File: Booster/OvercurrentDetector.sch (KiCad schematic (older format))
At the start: 37 parts

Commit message: Removed need for enable signal replacing it with a missing pulse detection RC based circuit.
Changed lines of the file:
@@
 Connection ~ 2650 6150
 Wire Wire Line
-	2650 6050 2650 6150
-Wire Wire Line
-	2650 6150 2650 6250
+	2650 6050 2650 6250
 Wire Wire Line
 	2750 1400 2600 1400
@@
 	2600 1400 2600 1200
 Wire Wire Line
-	3050 2900 3900 2900
+	3050 2900 4400 2900
 Wire Wire Line
-	3900 2900 4400 2900
-Wire Wire Line
-	4100 1350 4100 1400
-Wire Wire Line
-	4100 1400 4100 1650
+	4100 1350 4100 1650
 Wire Wire Line
 	4100 1050 4100 1000
 Wire Wire Line
-	4100 1000 4300 1000
-Wire Wire Line
-	4300 1000 4500 1000
-Wire Wire Line
-	4500 1000 8350 1000
+	4100 1000 8350 1000
 Wire Wire Line
 	4300 1000 4300 1050
@@
 	4100 1650 4150 1650
 Wire Wire Line
-	4300 1350 4300 1400
+	4300 1350 4300 1500
 Wire Wire Line
-	4300 1400 4300 1500
+	4300 1800 4300 1900
 Wire Wire Line
-	4300 1800 4300 1850
-Wire Wire Line
-	4300 1850 4300 1900
-Wire Wire Line
-	3350 1400 3450 1400
-Wire Wire Line
-	3450 1400 4100 1400
-Wire Wire Line
-	4100 1400 4300 1400
+	3350 1400 4300 1400
 Wire Wire Line
 	4500 1000 4500 1900
@@
 	4700 2100 4900 2100
 Wire Wire Line
-	4900 1850 4900 2100
-Wire Wire Line
-	4900 2100 4900 2250
+	4900 1850 4900 2250
 Connection ~ 4900 2100
 Wire Wire Line
 	4900 2750 4900 2550
 Wire Wire Line
-	3050 1700 3050 2900
+	3050 1700 3050 3450
 Wire Wire Line
-	3050 2900 3050 3450
+	3050 3750 3050 4000
 Wire Wire Line
-	3050 3750 3050 3900
-Wire Wire Line
-	3050 3900 3050 4000
-Wire Wire Line
-	3250 3750 3250 3900
-Wire Wire Line
-	3250 3900 3250 4000
+	3250 3750 3250 4000
 Wire Wire Line
 	3250 2050 3250 3450
@@
 	2650 5750 2650 5450
 Wire Wire Line
-	2500 6800 2500 7000
-Wire Wire Line
-	2500 7000 2500 7100
+	2500 6800 2500 7100
 Wire Wire Line
 	2650 6650 2650 6550
@@
 Connection ~ 3150 4800
 Wire Wire Line
-	4300 6050 4600 6050
+	4300 6050 5300 6050
 Wire Wire Line
-	4600 6050 5300 6050
-Wire Wire Line
-	4600 5600 4600 6050
-Wire Wire Line
-	4600 6050 4600 6200
+	4600 5600 4600 6200
 Connection ~ 4600 6050
 Wire Wire Line
@@
 	4600 6500 4600 6850
 Wire Wire Line
-	3150 4600 3150 4800
-Wire Wire Line
-	3150 4800 3150 5950
+	3150 4600 3150 5950
 Wire Wire Line
 	3150 5950 3700 5950
@@
 	3600 5700 3600 5600
 Wire Wire Line
-	3900 4950 3900 5150
-Wire Wire Line
-	3900 5150 3900 5750
+	3900 4950 3900 5750
 Wire Wire Line
 	3600 5300 3600 5150
@@
 	3900 6350 3900 6850
 Wire Wire Line
-	5900 5950 5950 5950
-Wire Wire Line
-	5950 5950 6850 5950
+	5900 5950 6850 5950
 Wire Wire Line
 	6850 5950 6850 4900
@@
 	8250 4000 8550 4000
 Wire Wire Line
-	8550 3850 8550 4000
-Wire Wire Line
-	8550 4000 8550 4100
+	8550 3850 8550 4100
 Connection ~ 8550 4000
 Wire Wire Line
@@
 	8750 5100 9000 5100
 Wire Wire Line
-	9000 4500 9000 5100
+	9000 4500 9000 5550
 Wire Wire Line
-	9000 5100 9000 5300
-Wire Wire Line
-	9000 5300 9000 5550
-Wire Wire Line
-	8750 5300 9000 5300
-Wire Wire Line
-	9000 5300 9200 5300
+	8750 5300 9200 5300
 Connection ~ 9000 5300
 Connection ~ 9000 5100
@@
 	9250 4150 9000 4150
 Wire Wire Line
-	9000 3850 9000 4150
-Wire Wire Line
-	9000 4150 9000 4200
+	9000 3850 9000 4200
 Connection ~ 9000 4150
 Wire Wire Line
 	7400 5800 7400 6000
 Wire Wire Line
-	7400 6000 8250 6000
+	7400 6000 9000 6000
 Wire Wire Line
-	8250 6000 9000 6000
-Wire Wire Line
-	8250 5500 8250 6000
-Wire Wire Line
-	8250 6000 8250 6150
+	8250 5500 8250 6150
 Connection ~ 8250 6000
 $Comp

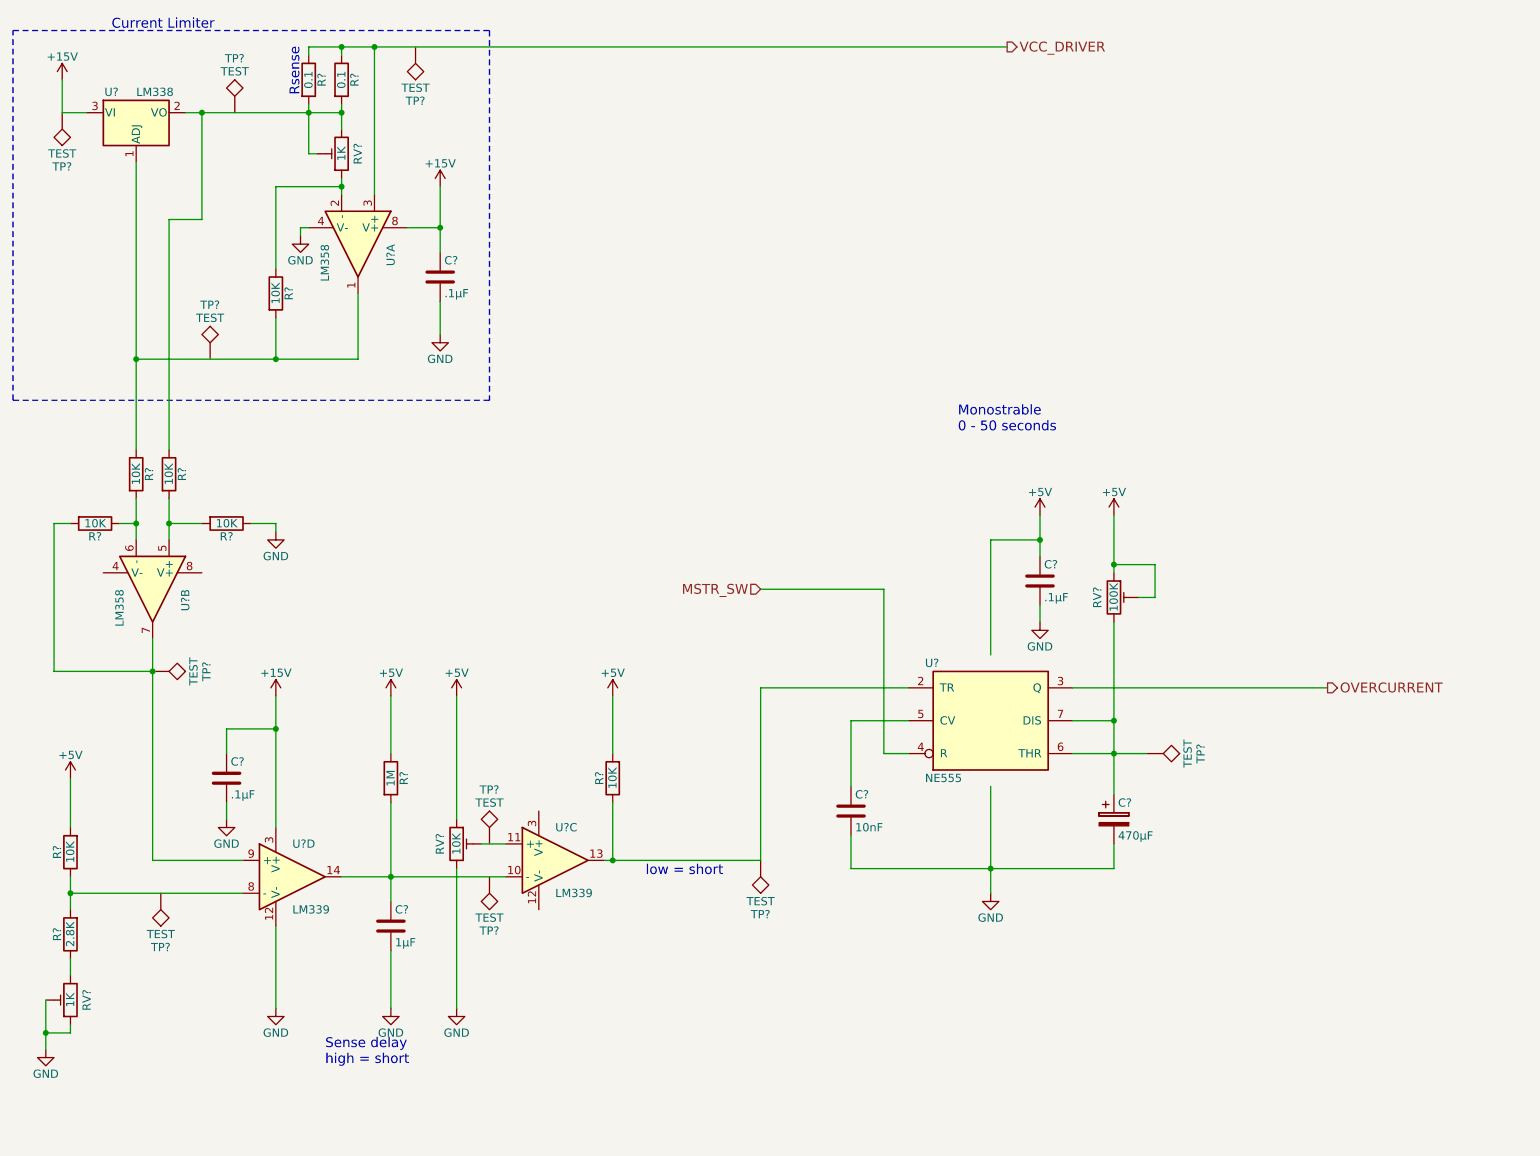
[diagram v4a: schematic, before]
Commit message: Fixed missing connections.
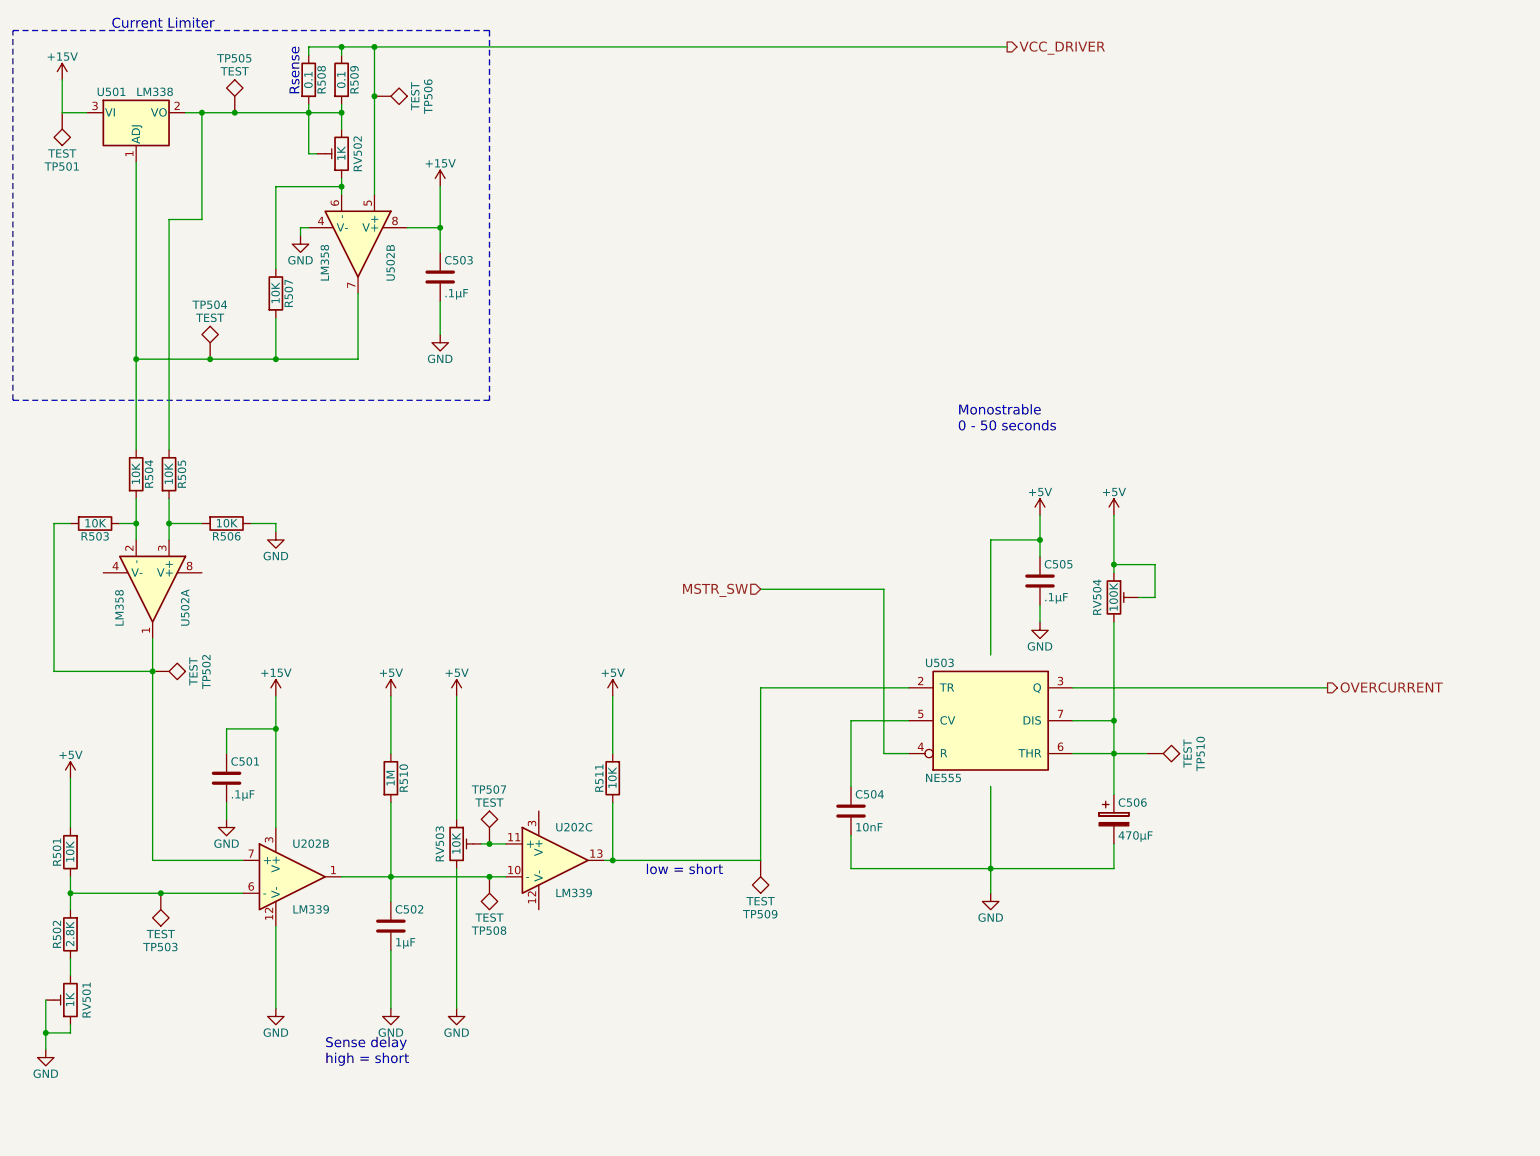
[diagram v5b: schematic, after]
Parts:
- gave numbers to parts that had none: 35
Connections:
- net VCC_DRIVER: now also TP506.1, U502.5 (+); no longer U502.3 (+)
- net at R501.1, R502.2: now also TP503.1, U202.6 (-); no longer U202.8 (-)
- net at R504.1, R507.2, U501.1 (ADJ): now also TP504.1, U502.7; no longer U502.1
- net at R505.1, R508.2, R509.2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: now also TP505.1
- net at R507.1, RV502.1: now also U502.6 (-); no longer U502.2 (-)
- net at R505.2, R506.2: now also U502.3 (+); no longer U502.5 (+)
- net at R503.1, R504.2: now also U502.2 (-); no longer U502.6 (-)
- net at R503.2, TP502.1: now also U202.7 (+), U502.1; no longer U202.9 (+), U502.7
- net at C502.1, R510.2, U202.10 (-): now also TP508.1, U202.1; no longer U202.14
- net at RV503.2, U202.11 (+): now also TP507.1
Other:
- moved on the sheet: TP506
